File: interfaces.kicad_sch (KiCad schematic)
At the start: 33 parts, among them J13 SM04B-SRSS-TB-LF-SN, J14 SM04B-SRSS-TB-LF-SN, J3 SI-51005-F, J8 Bus_M.2_MDT580M01001, U7 MAX3051EKA

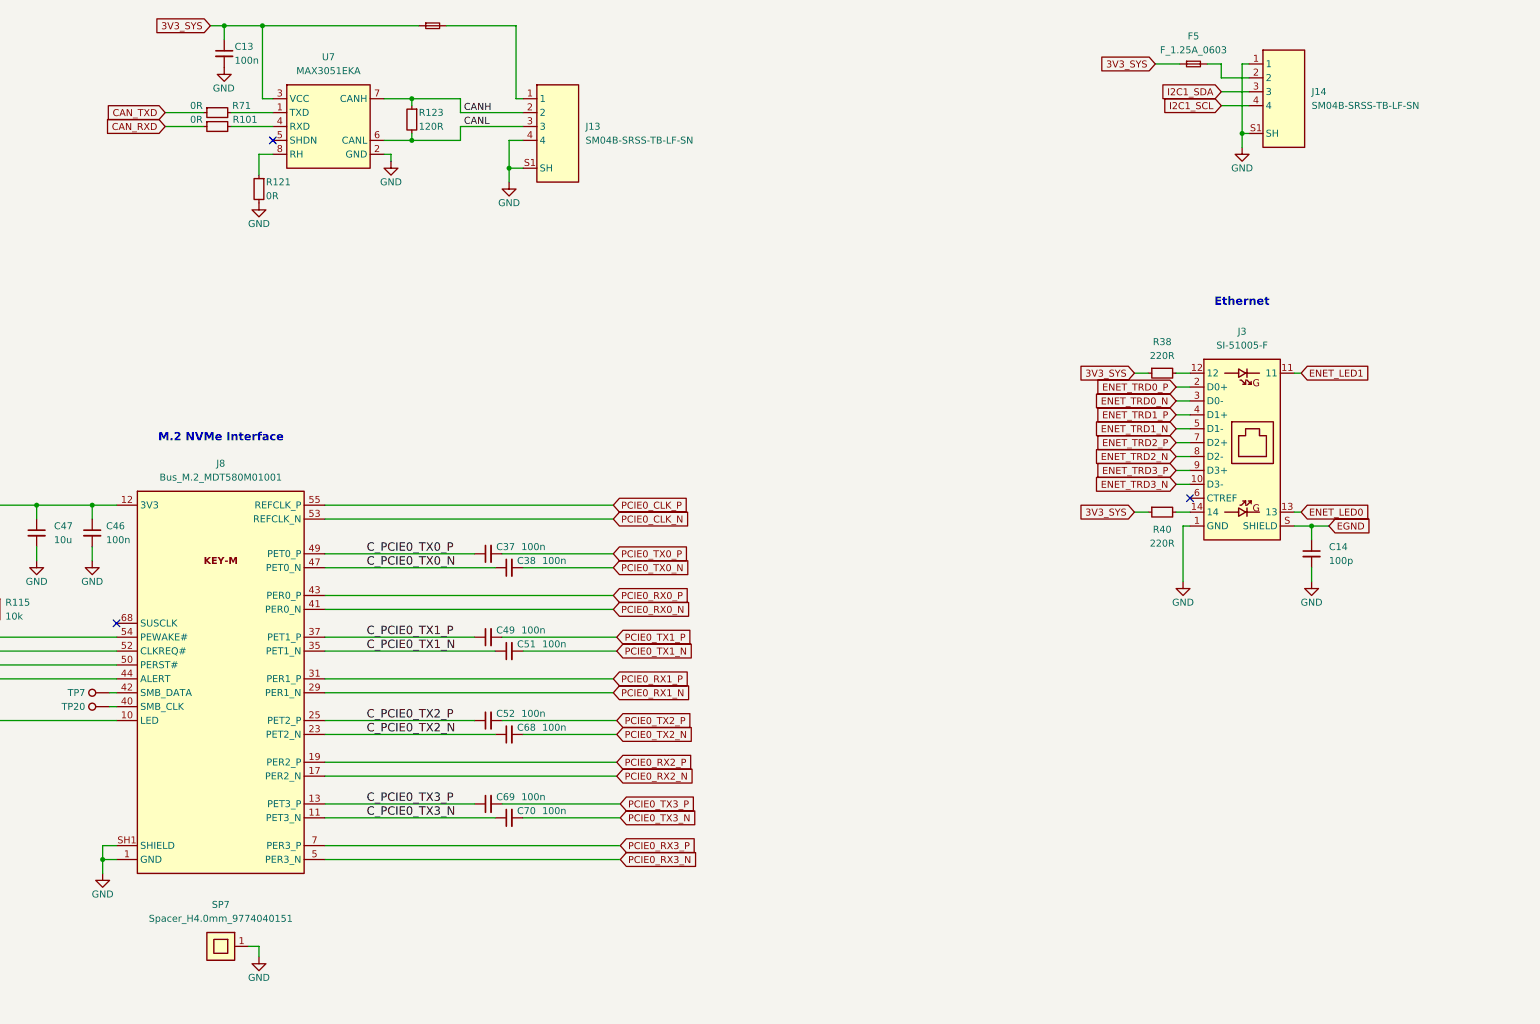
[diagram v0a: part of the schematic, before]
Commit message: [#56834] Fix components links
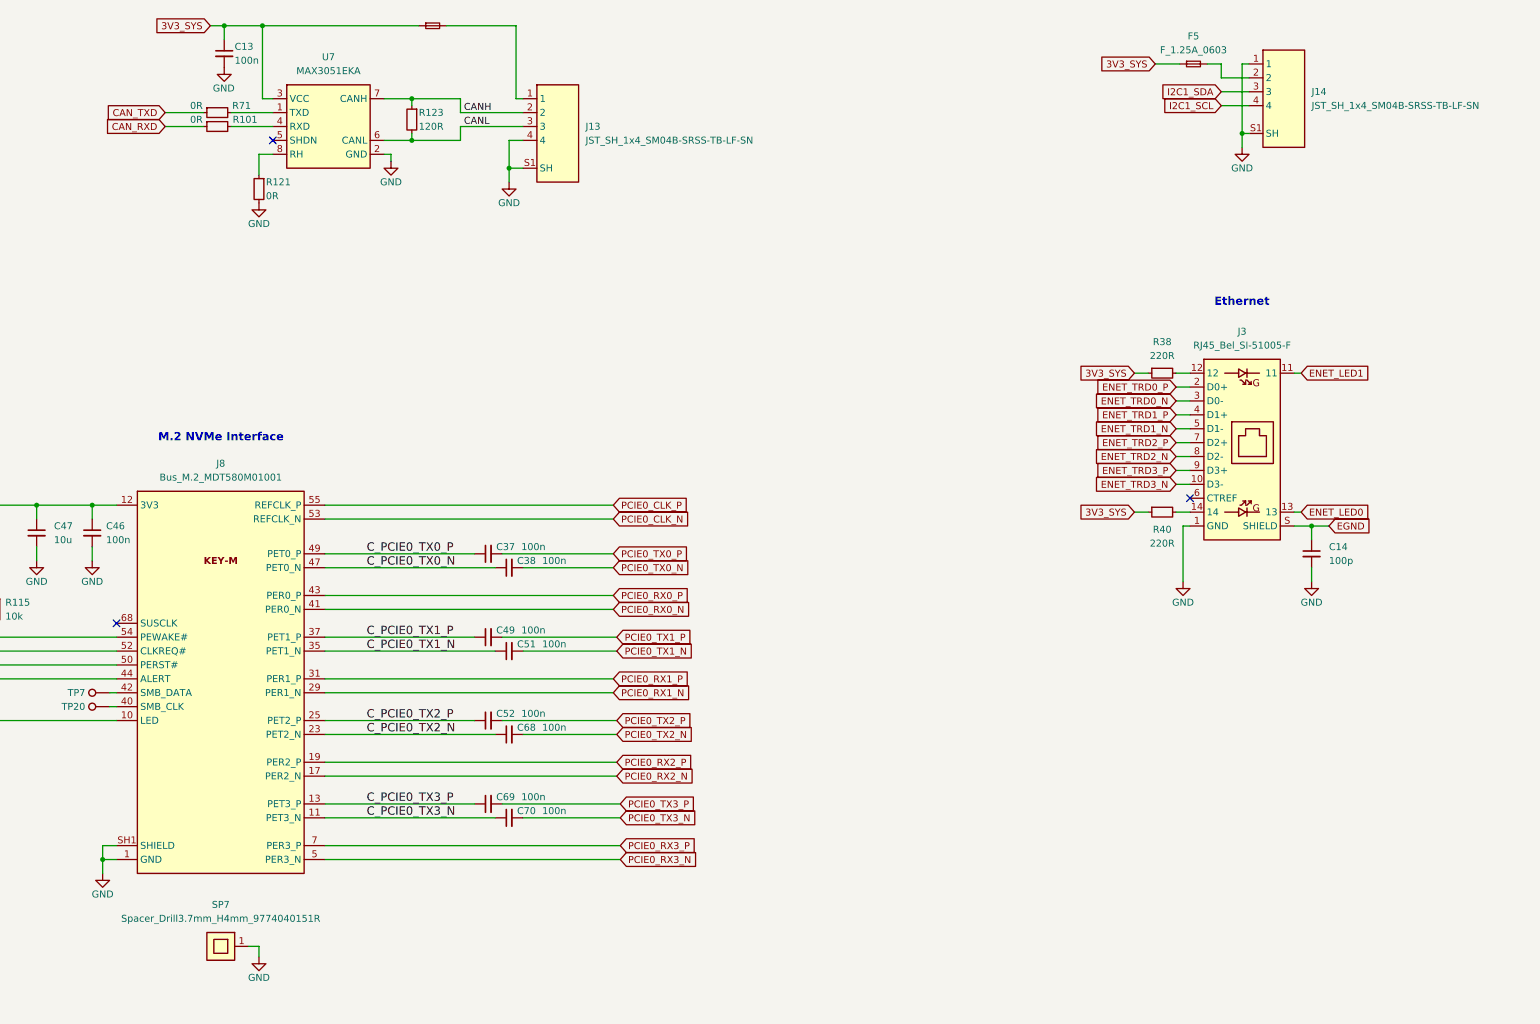
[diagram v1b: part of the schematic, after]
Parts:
- C13, C37, C38, C46, C49, C51, C52, C68, C69, C70: footprint antmicro-footprints:C_0402_1005Metric -> jetson-nano-baseboard-footprints:C_0402_1005Metric; symbol antmicroCapacitors0402:C_100n_0402 -> jetson-nano-baseboard:C_100n_0402
- C14: footprint antmicro-footprints:C_0402_1005Metric -> jetson-nano-baseboard-footprints:C_0402_1005Metric; symbol antmicroCapacitors0402:C_100p_0402 -> jetson-nano-baseboard:C_100p_0402
- C47: footprint antmicro-footprints:C_0603_1608Metric -> jetson-nano-baseboard-footprints:C_0603_1608Metric; symbol antmicroCapacitors0603:C_10u_0603 -> jetson-nano-baseboard:C_10u_0603
- F4, F5: footprint antmicro-footprints:F_0603_1608Metric -> jetson-nano-baseboard-footprints:F_0603_1608Metric; symbol antmicroFuses:F_1.25A_0603 -> jetson-nano-baseboard:F_1.25A_0603
- J13, J14: value SM04B-SRSS-TB-LF-SN -> JST_SH_1x4_SM04B-SRSS-TB-LF-SN; footprint antmicro-footprints:SM04B-SRSS-TB-LF-SN -> jetson-nano-baseboard-footprints:Conn_JST_SH_1x4_SM04B-SRSS-TB-LF-SN; symbol antmicroRectangularConnectorsHeadersMalePins:SM04B-SRSS-TB-LF-SN -> jetson-nano-baseboard:JST_SH_1x4_SM04B-SRSS-TB-LF-SN; Manufacturer JST -> JST Automotive Connectors
- J3: value SI-51005-F -> RJ45_Bel_SI-51005-F; footprint antmicro-footprints:RJ45_Bel_SI-51005-F -> jetson-nano-baseboard-footprints:RJ45_Bel_SI-51005-F; symbol antmicroModularConnectorsJacksWithMagnetics:RJ45_Bel_SI-51005-F -> jetson-nano-baseboard:RJ45_Bel_SI-51005-F; MPN SI-51005-F -> SI-51005-F; Manufacturer Bel Magnetic Solutions -> Bel Fuse
- J8: footprint antmicro-footprints:Bus_M.2_Socket_Key_M_Amphenol_MDT580M01001 -> jetson-nano-baseboard-footprints:Bus_M.2_Socket_Key_M_Amphenol_MDT580M01001; symbol antmicroPciConnectors:Bus_M.2_MDT580M01001 -> jetson-nano-baseboard:Bus_M.2_MDT580M01001
- NVME1: value ~ -> LED_G_0603_LG_L29K-G2J1-24-Z; footprint antmicro-footprints:LED_0603_1608Metric_G -> jetson-nano-baseboard-footprints:LED_0603_1608Metric_G; symbol antmicroLEDIndicationDiscrete:LED_G_0603_LG_L29K-G2J1-24-Z -> jetson-nano-baseboard:LED_G_0603_LG_L29K-G2J1-24-Z; Manufacturer Osram -> OSRAM
- R101, R121, R71: footprint antmicro-footprints:R_0402_1005Metric -> jetson-nano-baseboard-footprints:R_0402_1005Metric; symbol antmicroResistors0402:R_0R_0402 -> jetson-nano-baseboard:R_0R_0402
- R114, R115, R116: footprint antmicro-footprints:R_0402_1005Metric -> jetson-nano-baseboard-footprints:R_0402_1005Metric; symbol antmicroResistors0402:R_10k_0402 -> jetson-nano-baseboard:R_10k_0402
- R123: footprint antmicro-footprints:R_0402_1005Metric -> jetson-nano-baseboard-footprints:R_0402_1005Metric; symbol antmicroResistors0402:R_120R_0402 -> jetson-nano-baseboard:R_120R_0402
- R128, R38, R40: footprint antmicro-footprints:R_0402_1005Metric -> jetson-nano-baseboard-footprints:R_0402_1005Metric; symbol antmicroResistors0402:R_220R_0402 -> jetson-nano-baseboard:R_220R_0402
- SP7: value Spacer_H4.0mm_9774040151 -> Spacer_Drill3.7mm_H4mm_9774040151R; footprint antmicro-footprints:Spacer_SMD_M2.5_H4mm_Wurth_9774040151 -> jetson-nano-baseboard-footprints:Spacer_Drill3.7mm_H4mm_9774040151R; symbol antmicroMechanicalParts:Spacer_H4.0mm_9774040151 -> jetson-nano-baseboard:Spacer_Drill3.7mm_H4mm_9774040151R
- TP20, TP7: footprint antmicro-footprints:TP_SMD_1.5mm -> jetson-nano-baseboard-footprints:TP_SMD_1.5mm; symbol antmicroTestPoints:TP_1.5mm_SMD -> jetson-nano-baseboard:TP_1.5mm_SMD; MPN N/A -> (none); Manufacturer N/A -> (none)
- U7: footprint antmicro-footprints:SOT-23-8 -> jetson-nano-baseboard-footprints:SOT-23-8; symbol antmicroInterfaceDriversReceiversTransceivers:MAX3051EKA -> jetson-nano-baseboard:MAX3051EKA; Manufacturer Maxim Integrated -> Maxim Integrated Products

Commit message: [#57913] fix 2309413-1
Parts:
- C13, C37, C38, C46, C49, C51, C52, C68, C69, C70: footprint jetson-nano-baseboard-footprints:C_0402_1005Metric -> antmicro-footprints:C_0402_1005Metric; symbol jetson-nano-baseboard:C_100n_0402 -> antmicroCapacitors0402:C_100n_0402
- C14: footprint jetson-nano-baseboard-footprints:C_0402_1005Metric -> antmicro-footprints:C_0402_1005Metric; symbol jetson-nano-baseboard:C_100p_0402 -> antmicroCapacitors0402:C_100p_0402
- C47: footprint jetson-nano-baseboard-footprints:C_0603_1608Metric -> antmicro-footprints:C_0603_1608Metric; symbol jetson-nano-baseboard:C_10u_0603 -> antmicroCapacitors0603:C_10u_0603
- F4, F5: footprint jetson-nano-baseboard-footprints:F_0603_1608Metric -> antmicro-footprints:F_0603_1608Metric; symbol jetson-nano-baseboard:F_1.25A_0603 -> antmicroFuses:F_1.25A_0603
- J13, J14: footprint jetson-nano-baseboard-footprints:Conn_JST_SH_1x4_SM04B-SRSS-TB-LF-SN -> antmicro-footprints:Conn_JST_SH_1x4_SM04B-SRSS-TB-LF-SN; symbol jetson-nano-baseboard:JST_SH_1x4_SM04B-SRSS-TB-LF-SN -> antmicroWire2BoardConnectors:JST_SH_1x4_SM04B-SRSS-TB-LF-SN
- J3: footprint jetson-nano-baseboard-footprints:RJ45_Bel_SI-51005-F -> antmicro-footprints:RJ45_Bel_SI-51005-F; symbol jetson-nano-baseboard:RJ45_Bel_SI-51005-F -> antmicroModularConnectorsJacksWithMagnetics:RJ45_Bel_SI-51005-F
- J8: footprint jetson-nano-baseboard-footprints:Bus_M.2_Socket_Key_M_Amphenol_MDT580M01001 -> antmicro-footprints:Bus_M.2_Socket_Key_M_Amphenol_MDT580M01001; symbol jetson-nano-baseboard:Bus_M.2_MDT580M01001 -> antmicroPciConnectors:Bus_M.2_MDT580M01001
- NVME1: footprint jetson-nano-baseboard-footprints:LED_0603_1608Metric_G -> antmicro-footprints:LED_0603_1608Metric_G; symbol jetson-nano-baseboard:LED_G_0603_LG_L29K-G2J1-24-Z -> antmicroLEDIndicationDiscrete:LED_G_0603_LG_L29K-G2J1-24-Z
- R101, R121, R71: footprint jetson-nano-baseboard-footprints:R_0402_1005Metric -> antmicro-footprints:R_0402_1005Metric; symbol jetson-nano-baseboard:R_0R_0402 -> antmicroResistors0402:R_0R_0402
- R114, R115, R116: footprint jetson-nano-baseboard-footprints:R_0402_1005Metric -> antmicro-footprints:R_0402_1005Metric; symbol jetson-nano-baseboard:R_10k_0402 -> antmicroResistors0402:R_10k_0402
- R123: footprint jetson-nano-baseboard-footprints:R_0402_1005Metric -> antmicro-footprints:R_0402_1005Metric; symbol jetson-nano-baseboard:R_120R_0402 -> antmicroResistors0402:R_120R_0402
- R128, R38, R40: footprint jetson-nano-baseboard-footprints:R_0402_1005Metric -> antmicro-footprints:R_0402_1005Metric; symbol jetson-nano-baseboard:R_220R_0402 -> antmicroResistors0402:R_220R_0402
- SP7: footprint jetson-nano-baseboard-footprints:Spacer_Drill3.7mm_H4mm_9774040151R -> antmicro-footprints:Spacer_Drill3.7mm_H4mm_9774040151R; symbol jetson-nano-baseboard:Spacer_Drill3.7mm_H4mm_9774040151R -> antmicroMechanicalParts:Spacer_Drill3.7mm_H4mm_9774040151R
- TP20, TP7: footprint jetson-nano-baseboard-footprints:TP_SMD_1.5mm -> antmicro-footprints:TP_SMD_1.5mm; symbol jetson-nano-baseboard:TP_1.5mm_SMD -> antmicroTestPoints:TP_1.5mm_SMD
- U7: footprint jetson-nano-baseboard-footprints:SOT-23-8 -> antmicro-footprints:SOT-23-8; symbol jetson-nano-baseboard:MAX3051EKA -> antmicroInterfaceDriversReceiversTransceivers:MAX3051EKA

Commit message: [#83358] Update KiCad project files
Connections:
- net GND: no longer J13.S1 (SH), J13.S2 (SH), J14.S1 (SH), J14.S2 (SH)
- net at NVME1.2 (A): no longer J8.10 (LED)
- now unconnected: J8.20 (NC), J8.22 (NC), J8.24 (NC), J8.26 (NC), J8.28 (NC), J8.30 (NC), J8.32 (NC), J8.34 (NC), J8.36 (NC), J8.38 (NC), J8.46 (NC), J8.48 (NC), J8.56 (NC), J8.58 (NC), J8.6 (NC), J8.67 (NC), J8.69 (NC), J8.8 (NC)

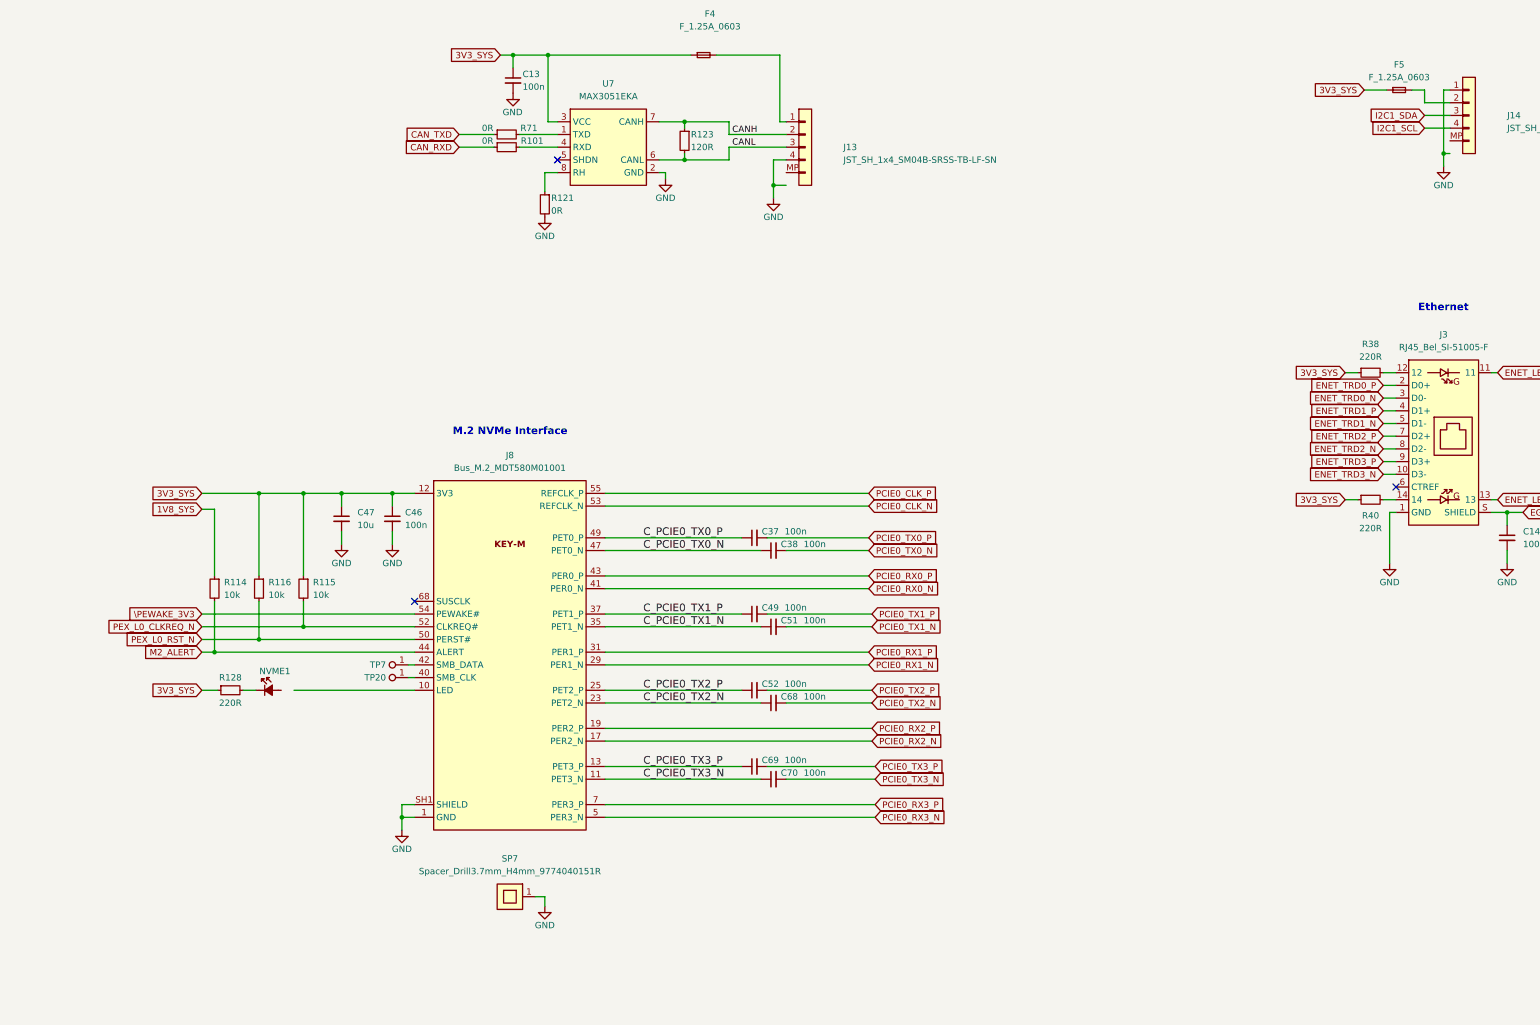
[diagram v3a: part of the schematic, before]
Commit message: [#83358] Repair broken symbol after update
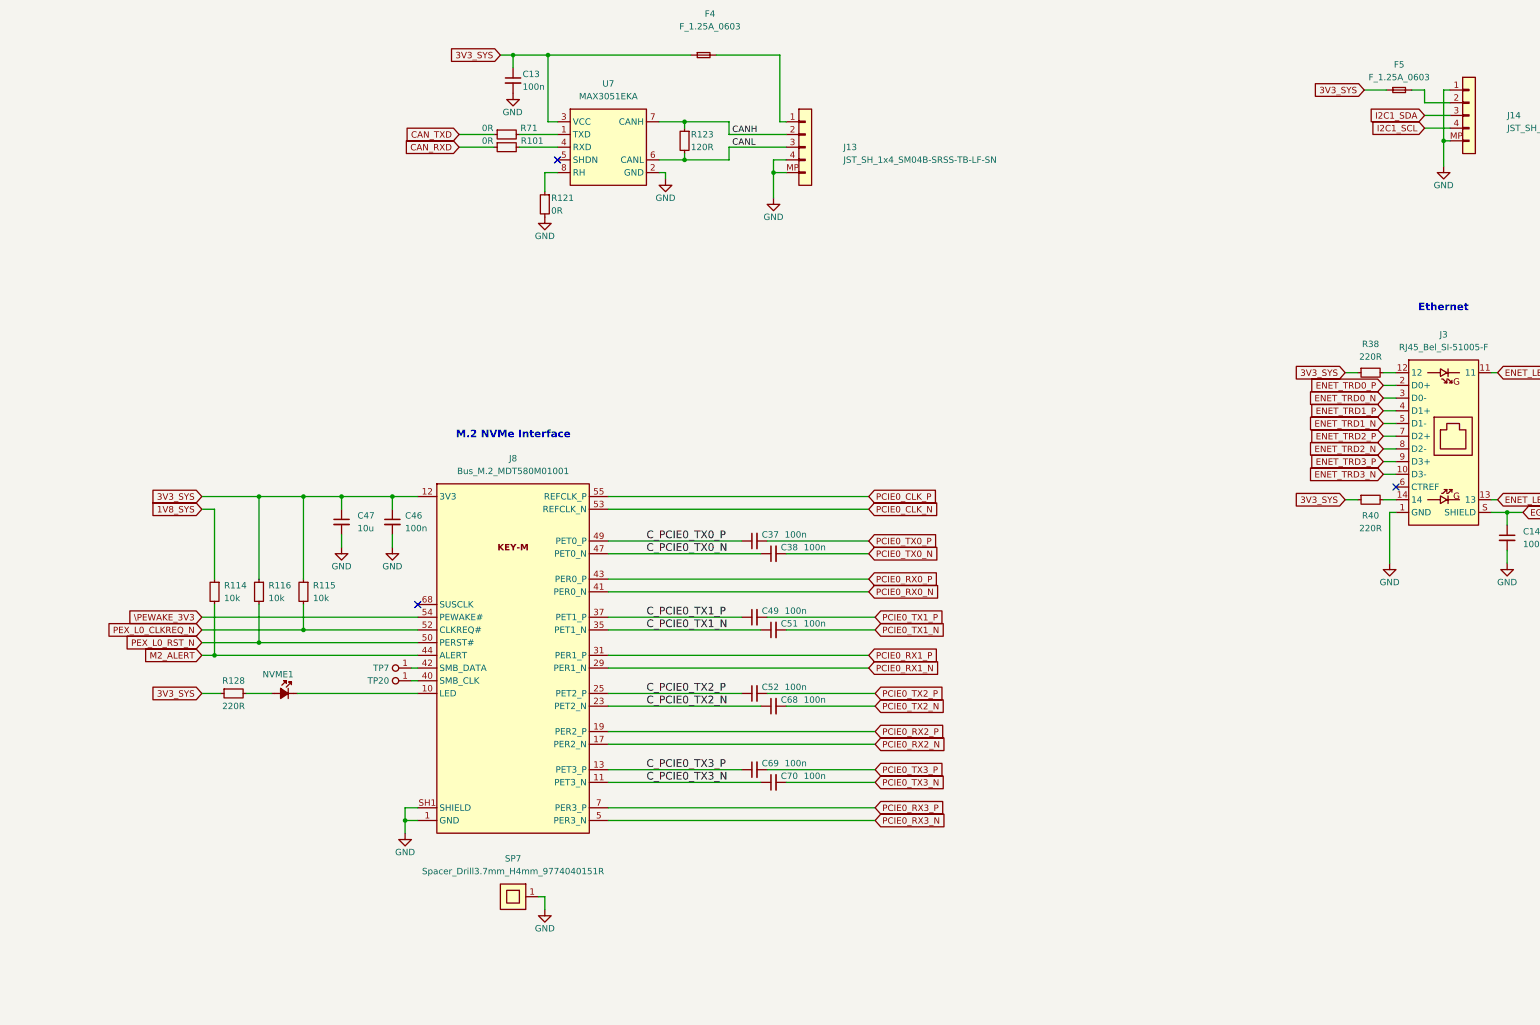
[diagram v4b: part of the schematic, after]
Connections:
- net GND: now also J13.MP, J14.MP
- net at NVME1.1 (C): now also J8.10 (LED); no longer R128.2
- net at NVME1.2 (A): now also R128.2
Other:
- moved on the sheet: C37, C38, C46, C47, C49, C51, C52, C68, C69, C70, J8, NVME1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
